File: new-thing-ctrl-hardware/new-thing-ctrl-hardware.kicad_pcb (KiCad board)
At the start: 2 copper layers, 132 x 80 mm, 43 parts, among them J1 MSTBAish, J10 MSTBAish, J11 Neopixels, J2 MSTBAish, J3 SD, J4 MFRC522, J5 Conn_01x04_Male, J6 Screw_Terminal_01x09, J7 LCD, J8 Screw_Terminal_01x06, J9 Screw_Terminal_01x06, Q1 TIP120, Q2 TIP120, SW1 6X6, SW2 6X6, SW3 6X6, SW4 6X6, U1 L7805, U2 Pico

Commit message: routed
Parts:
- added C8: 100n, Capacitor_THT:C_Disc_D7.0mm_W2.5mm_P5.00mm, B.Cu at (163.8, 98.8)
- added C9: 10u, Capacitor_THT:CP_Radial_D5.0mm_P2.50mm, B.Cu at (177.0, 104.9)
- SW1, SW2, SW3, SW4: footprint Button_Switch_THT:SW_PUSH_6mm_H7.3mm -> Button_Switch_THT:SW_PUSH_6mm_H13mm
- moved J11 29.7 mm to (184.3, 100.1), turned to -90 degrees
- moved C5 6.65 mm to (86.1, 38.6), turned to -90 degrees
- moved D5 6.55 mm to (161.3, 94.5), turned to 180 degrees
- moved C1 3.98 mm to (154.7, 45.2)
- moved R1 2.29 mm to (148.8, 39.9)
- moved R2 2.29 mm to (148.8, 42.2)
- moved C6 1.69 mm to (81.3, 86.6)
- moved H3 1.00 mm to (159.0, 88.0)
- moved H4 1.00 mm to (87.0, 88.0)
- moved SW1 0.75 mm to (92.8, 85.0)
- moved SW2 0.75 mm to (110.8, 85.0)
- moved SW3 0.75 mm to (128.8, 85.0)
- moved SW4 0.75 mm to (146.8, 85.0)
- moved J10 0.25 mm to (182.0, 87.9)
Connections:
- D5 pad 1: +3V3 -> +5V
- J11 pad 3: +3V3 -> +5V
- J3 pad 4: /SPI_CLK -> /SPI_SCK
- J6 pad 5: /ADC_1 -> /ADC_0
- J6 pad 7: /ADC_0 -> /ADC_2
- J8 pad 2: /SPI_SCK -> /SPI_RX
- J8 pad 3: /SPI_RX -> /SPI_SCK
- U2 pad 1: /BUT_0 -> /SPI_CS_LCD
- U2 pad 10: /TCH_IRQ -> /COIL_0
- U2 pad 11: /LCD_RST -> /COIL_1
- U2 pad 12: /LCD_DC/RS -> /NEOPIXEL
- U2 pad 14: /LCD_BACKLIGHT -> /BUT_1
- U2 pad 15: /NFC_IRQ -> /BUT_0
- U2 pad 16: /COIL_0 -> /BUT_3
- U2 pad 17: /COIL_1 -> /BUT_2
- U2 pad 2: /BUT_1 -> /LCD_RST
- U2 pad 22: /SPI_CS_LCD -> /NFC_RST
- U2 pad 26: /NFC_RST -> /TCH_IRQ
- U2 pad 29: /NEOPIXEL -> /SPI_CS_TCH
- U2 pad 4: /BUT_2 -> /LCD_DC/RS
- U2 pad 5: /BUT_3 -> /LCD_BACKLIGHT
- U2 pad 9: /SPI_CS_TCH -> /SPI_CS_SD
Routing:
- net +5V: track 0.00 -> 275.6 mm
- net +3V3: track 0.00 -> 185.5 mm
- net /SPI_TX: track 0.00 -> 148.6 mm, vias 0 -> 9
- net /SPI_SCK: track 0.00 -> 144.3 mm, vias 0 -> 5
- net /SPI_RX: track 0.00 -> 141.9 mm, vias 0 -> 8
- net /D14: track 0.00 -> 139.6 mm, vias 0 -> 6
- net +24V: track 0.00 -> 137.7 mm
- net /ADC_2: track 0.00 -> 104.7 mm
- net /ADC_1: track 0.00 -> 67.8 mm, vias 0 -> 2
- net /BUT_0: track 0.00 -> 65.7 mm, vias 0 -> 1
- net /NEOPIXEL: track 0.00 -> 64.4 mm, vias 0 -> 3
- net /LCD_BACKLIGHT: track 0.00 -> 60.9 mm
- net /ADC_0: track 0.00 -> 60.8 mm, vias 0 -> 2
- net /COIL_1: track 0.00 -> 57.0 mm, vias 0 -> 4
- net /LCD_DC/RS: track 0.00 -> 55.9 mm
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- added copper zone on B.Cu, net GND
- added copper zone on In1.Cu, net GND
- added copper zone on In2.Cu, net GND
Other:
- copper layers 2 -> 4

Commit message: ready for review and manufacture
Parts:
- added J12: EXP1, Connector_Phoenix_MSTB:PhoenixContact_MSTBA_2,5_6-G-5,08_1x06_P5.08mm_Horizontal, B.Cu at (75.8, 97.2)
- added R5: 100K, Resistor_THT:R_Axial_DIN0204_L3.6mm_D1.6mm_P7.62mm_Horizontal, B.Cu at (168.0, 58.7)
- added R6: 100K, Resistor_THT:R_Axial_DIN0204_L3.6mm_D1.6mm_P7.62mm_Horizontal, B.Cu at (168.1, 82.8)
- J4: value MFRC522 -> PN532; footprint Connector_JST:JST_XH_S8B-XH-A_1x08_P2.50mm_Horizontal -> Connector_JST:JST_XH_S4B-XH-A_1x04_P2.50mm_Horizontal
- J5: footprint Connector_JST:JST_XH_B4B-XH-A_1x04_P2.50mm_Vertical -> Connector_JST:JST_XH_S4B-XH-A_1x04_P2.50mm_Horizontal
- J6: value Screw_Terminal_01x09 -> EXP0; footprint Connector_Phoenix_MSTB:PhoenixContact_MSTBA_2,5_9-G-5,08_1x09_P5.08mm_Horizontal -> Connector_Phoenix_MSTB:PhoenixContact_MSTBA_2,5_6-G-5,08_1x06_P5.08mm_Horizontal
- moved J4 54.1 mm to (94.2, 37.7), turned to 0 degrees
- moved C6 44.6 mm to (96.7, 44.8), turned to 180 degrees
- moved R2 16.9 mm to (135.2, 32.2), turned to -90 degrees
- moved H3 16.3 mm to (154.0, 103.5)
- moved R1 12.8 mm to (137.5, 33.9), turned to -90 degrees
- moved J5 7.63 mm to (141.8, 37.8), turned to 0 degrees
- moved J6 0.68 mm to (109.0, 94.0)
- moved H1 0.50 mm to (169.5, 44.0)
- moved J8 0.09 mm to (75.8, 63.7)
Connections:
- J4 pad 1: +3V3 -> GND
- J4 pad 2: /NFC_RST -> +3V3
- J4 pad 3: GND -> /SDA
- J4 pad 4: /NFC_IRQ -> /SCL
- J6 pad 2: GND -> /ADC_0
- J6 pad 3: /D15 -> /ADC_1
- J6 pad 4: /D14 -> /ADC_2
- J6 pad 5: /ADC_0 -> +3V3
- J6 pad 6: /ADC_1 -> +5V
- U2 pad 22: /NFC_RST -> /D17
- U2 pad 27: /SPI_CS_NFC -> /SPI_CS_TCH
- U2 pad 29: /SPI_CS_TCH -> /D22
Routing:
- net /D22: track 0.00 -> 60.7 mm, vias 0 -> 2
- net /D14: track 139.6 -> 87.5 mm, vias 6 -> 4
- net /D17: track 0.00 -> 50.1 mm, vias 0 -> 2
- net /SCL: track 31.2 -> 74.5 mm, vias 0 -> 1
- net /NFC_RST: track 43.0 -> 0.00 mm
- net /ADC_2: track 104.7 -> 63.6 mm, vias 0 -> 1
- net /SPI_CS_NFC: track 41.0 -> 0.00 mm
- net /SDA: track 29.4 -> 68.2 mm
- net +3V3: track 185.5 -> 163.6 mm
- net +5V: track 275.6 -> 295.9 mm
- net /ADC_0: track 60.8 -> 46.4 mm, vias 2 -> 1
- net /ADC_1: track 67.8 -> 55.5 mm, vias 2 -> 1
- net /SPI_TX: track 148.6 -> 137.3 mm, vias 9 -> 8
- net /LCD_RST: track 52.6 -> 57.0 mm
- net Net-(Q1-Pad1): track 2.45 -> 6.33 mm
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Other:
- board size 132 x 80 mm -> 135.2 x 80 mm
- board text added: "- COIL0 +"
- board text added: "- COIL1 +"
- board text added: "12-24V IN"
- board text added: "3V3"
- board text added: "5V"
- board text added: "ADC0"
- board text added: "ADC1"
- board text added: "ADC2"
- board text added: "BUT0"
- board text added: "BUT1"
- board text added: "BUT2"
- board text added: "BUT3"
- board text added: "BUTTON EXPANSION"
- board text added: "CLK"
- board text added: "D14"
- board text added: "D15"
- board text added: "D17"
- board text added: "D22"
- board text added: "GND"
- board text added: "GND +"
- board text added: "GPIO EXPANSION"
- board text added: "I2C"
- board text added: "NEOPIXEL 5V DAT GND"
- board text added: "PN532/I2C"
- board text added: "RX"
- board text added: "SCL"
- board text added: "SDA"
- board text added: "SPI EXPANSION"
- board text added: "TX"

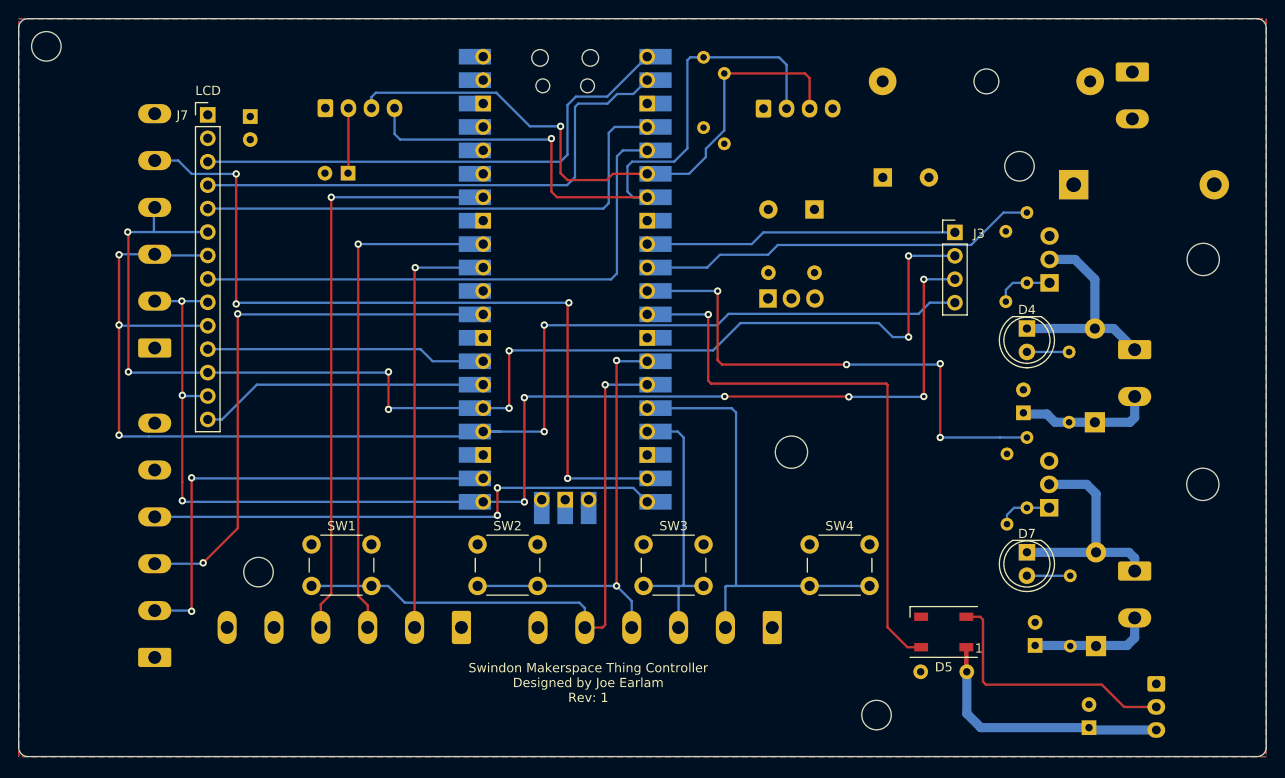
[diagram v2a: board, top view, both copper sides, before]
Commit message: changed some connector footprints, added reset button
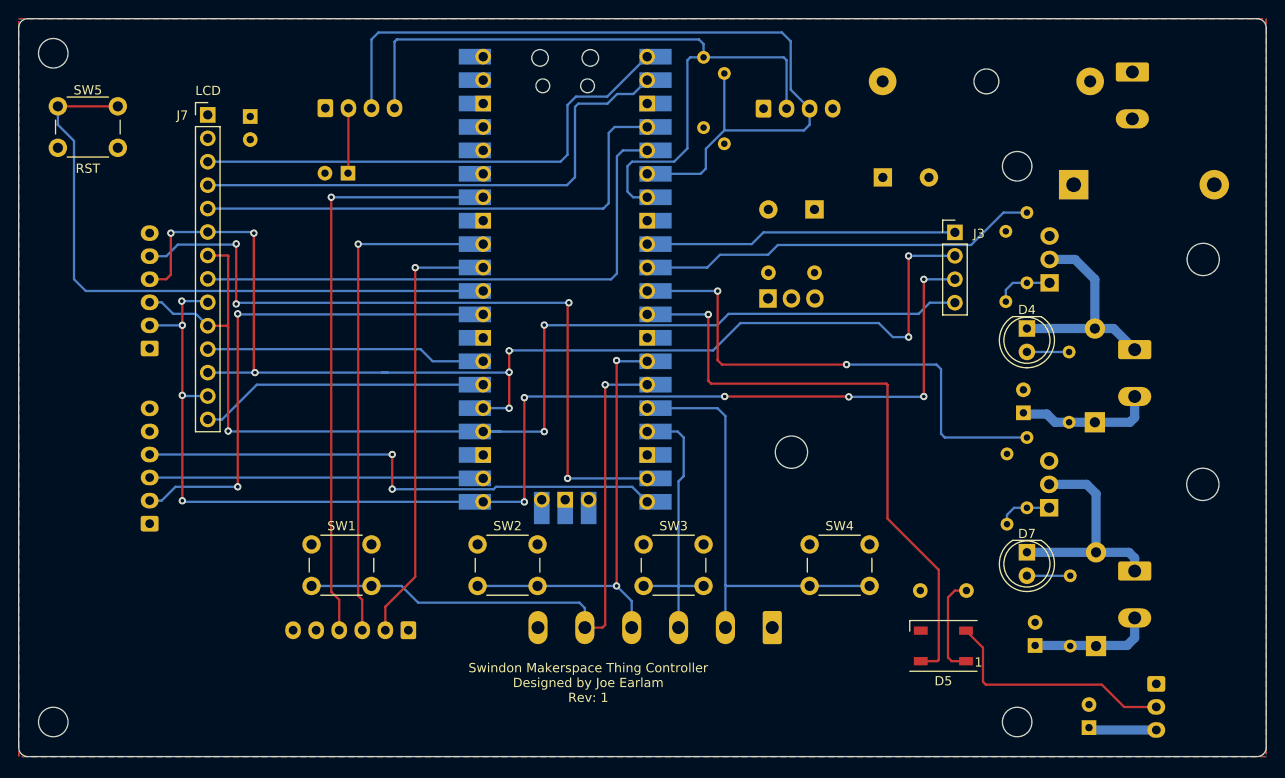
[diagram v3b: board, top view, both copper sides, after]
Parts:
- added SW5: 6X6, Button_Switch_THT:SW_PUSH_6mm_H4.3mm, F.Cu at (71.8, 42.0)
- J12: value EXP1 -> Conn_01x06_Male; footprint Connector_Phoenix_MSTB:PhoenixContact_MSTBA_2,5_6-G-5,08_1x06_P5.08mm_Horizontal -> Connector_JST:JST_XH_S6B-XH-A_1x06_P2.50mm_Horizontal
- J6: value EXP0 -> Conn_01x06_Male; footprint Connector_Phoenix_MSTB:PhoenixContact_MSTBA_2,5_6-G-5,08_1x06_P5.08mm_Horizontal -> Connector_JST:JST_XH_S6B-XH-A_1x06_P2.50mm_Horizontal
- J8: value Screw_Terminal_01x06 -> Conn_01x06_Male; footprint Connector_Phoenix_MSTB:PhoenixContact_MSTBA_2,5_6-G-5,08_1x06_P5.08mm_Horizontal -> Connector_JST:JST_XH_S6B-XH-A_1x06_P2.50mm_Horizontal
- R4, R8: value 1K -> 3K
- moved H4 27.6 mm to (64.8, 104.2)
- moved H3 15.3 mm to (169.2, 104.2)
- moved J12 14.5 mm to (75.2, 82.8)
- moved C8 8.81 mm to (163.8, 90.0)
- moved J6 5.76 mm to (103.2, 94.3)
- moved D5 1.51 mm to (161.2, 96.0)
- moved H2 1.06 mm to (64.8, 31.8)
- moved J8 0.55 mm to (75.2, 63.8)
- moved H1 0.25 mm to (169.2, 44.0)
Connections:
- J12 pad 2: /D17 -> /D22
- J12 pad 3: /D22 -> /D17
- U2 pad 30: unconnected-(U2-Pad30) -> Net-(U2-Pad30)
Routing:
- net Net-(U2-Pad30): track 0.00 -> 70.9 mm
- net /SDA: track 68.2 -> 90.7 mm, vias 1 -> 0
- net /SPI_SCK: track 144.3 -> 124.2 mm, vias 5 -> 3
- net /D17: track 50.1 -> 36.2 mm, vias 2 -> 0
- net +3V3: track 163.6 -> 173.4 mm
- net +5V: track 295.9 -> 305.5 mm
- net /D14: track 87.5 -> 80.3 mm
- net /SCL: track 74.5 -> 80.7 mm, vias 1 -> 0
- net /D22: track 60.7 -> 55.8 mm
- net /SPI_TX: track 137.3 -> 132.6 mm
- net /NEOPIXEL: track 64.3 -> 67.6 mm
- net Net-(D5-Pad2): track 28.6 -> 26.2 mm
- net /ADC_0: track 46.4 -> 48.1 mm
- net /D15: track 57.1 -> 58.5 mm
- net /BUT_3: track 48.7 -> 47.4 mm
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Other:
- board text added: "D0 LCD CS D1 LCD RST D2 LCD DC/RS D3 LCD BLIGHT D6 SD CS D7 COIL 0 D8 COIL 1 D9 NEOPIXEL D10 BUT1 D11 BUT0 D12 BUT3 D13 BUT2 D20 TCH IRQ D21 TCH CS"
- board text added: "I2C EXPANSION"
- board text added: "RST"
- board text removed: "I2C"
